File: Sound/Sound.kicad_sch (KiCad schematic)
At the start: 78 parts, among them J1 Buss, J2 Audio Out, SW1 Slot, U1 YM2149, U2 74LS85, U3 74LS00, U4 SAA1099, U5 74LS139, U6 YM2149, U7 SAA1099, U8 MCP6002, U9 74LS74, Y1 8MHz

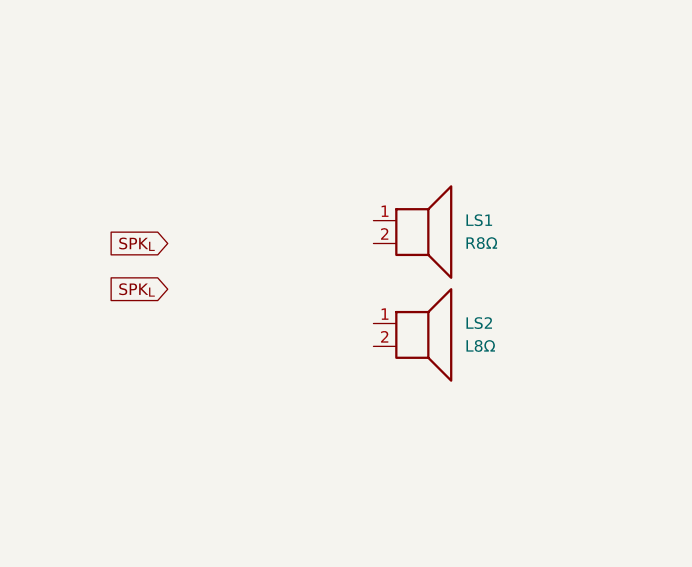
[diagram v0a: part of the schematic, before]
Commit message: outputs to terminal/log file
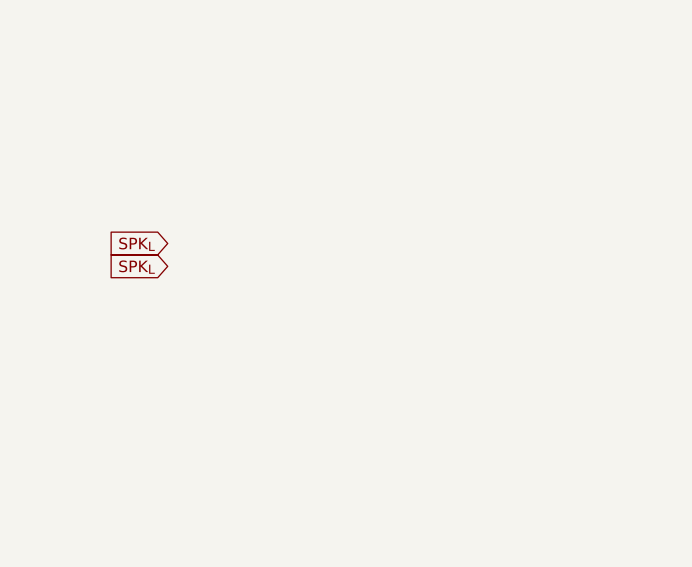
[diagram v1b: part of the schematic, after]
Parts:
- removed LS1: R8Ω, symbol Device:Speaker
- removed LS2: L8Ω, symbol Device:Speaker
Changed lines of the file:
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@@
 	(global_label "SPK_{L}"
 		(shape input)
-		(at 33.02 176.53 180)
+		(at 33.02 173.99 180)
 		(fields_autoplaced yes)
 		(effects
@@
 		)
 		(property "Intersheetrefs" "${INTERSHEET_REFS}"
-			(at 25.412 176.53 0)
+			(at 25.412 173.99 0)
 			(effects
 				(font
@@
 	)
 	(symbol
-		(lib_id "Device:Speaker")
-		(at 60.96 180.34 0)
-		(unit 1)
-		(exclude_from_sim no)
-		(in_bom yes)
-		(on_board yes)
-		(dnp no)
-		(fields_autoplaced yes)
-		(property "Reference" "LS2"
-			(at 66.04 180.3399 0)
-			(effects
-				(font
-					(size 1.27 1.27)
-				)
-				(justify left)
-			)
-		)
-		(property "Value" "L8Ω"
-			(at 66.04 182.8799 0)
-			(effects
-				(font
-					(size 1.27 1.27)
-				)
-				(justify left)
-			)
-		)
-		(property "Footprint" ""
-			(at 60.96 185.42 0)
-			(effects
-				(font
-					(size 1.27 1.27)
-				)
-				(hide yes)
-			)
-		)
-		(property "Datasheet" "~"
-			(at 60.706 181.61 0)
-			(effects
-				(font
-					(size 1.27 1.27)
-				)
-				(hide yes)
-			)
-		)
-		(property "Description" "Speaker"
-			(at 60.96 180.34 0)
-			(effects
-				(font
-					(size 1.27 1.27)
-				)
-				(hide yes)
-			)
-		)
-		(pin "1"
-		)
-		(pin "2"
-		)
-		(instances
-			(project "Sound"
-				(path "/e0d1fb1e-fa63-41d1-b097-e8f57c1048de"
-					(reference "LS2")
-					(unit 1)
-				)
-			)
-		)
-	)
-	(symbol
 		(lib_id "74xx:74LS00")
 		(at 160.02 128.27 0)
@@
 					(unit 1)
 				)
-			)
-		)
-	)
-	(symbol
-		(lib_id "Device:Speaker")
-		(at 60.96 168.91 0)
-		(unit 1)
-		(exclude_from_sim no)
-		(in_bom yes)
-		(on_board yes)
-		(dnp no)
-		(fields_autoplaced yes)
-		(property "Reference" "LS1"
-			(at 66.04 168.9099 0)
-			(effects
-				(font
-					(size 1.27 1.27)
-				)
-				(justify left)
-			)
-		)
-		(property "Value" "R8Ω"
-			(at 66.04 171.4499 0)
-			(effects
-				(font
-					(size 1.27 1.27)
-				)
-				(justify left)
-			)
-		)
-		(property "Footprint" ""
-			(at 60.96 173.99 0)
-			(effects
-				(font
-					(size 1.27 1.27)
-				)
-				(hide yes)
-			)
-		)
-		(property "Datasheet" "~"
-			(at 60.706 170.18 0)
-			(effects
-				(font
-					(size 1.27 1.27)
-				)
-				(hide yes)
-			)
-		)
-		(property "Description" "Speaker"
-			(at 60.96 168.91 0)
-			(effects
-				(font
-					(size 1.27 1.27)
-				)
-				(hide yes)
-			)
-		)
-		(pin "1"
-		)
-		(pin "2"
-		)
-		(instances
-			(project ""
-				(path "/e0d1fb1e-fa63-41d1-b097-e8f57c1048de"
-					(reference "LS1")
-					(unit 1)
-				)
